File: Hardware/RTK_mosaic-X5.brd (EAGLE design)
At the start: 151.8 x 101.6 mm, 359 parts, among them J2 MAGJACK-POE, J3 MICRO-SD-PUSH-PUSH-EXT-PIN, J4 Vertical Qwiic Connector, J9 MAGJACK-POE, U1 ESP32-WROVER-IE, U10 POE_PSU-DP990X, U11 SN74AVC4T774PW, U17 URB2405YMD, U2 CH340C, U3 AP7361C-33FGEUDFN-8, U4 TXS0108, U5 TXS0108, U6 AP7361C-33FGEUDFN-8, U7 KSZ8041NL, U8 MOSAIC-X5X5, U9 KSZ8041NL

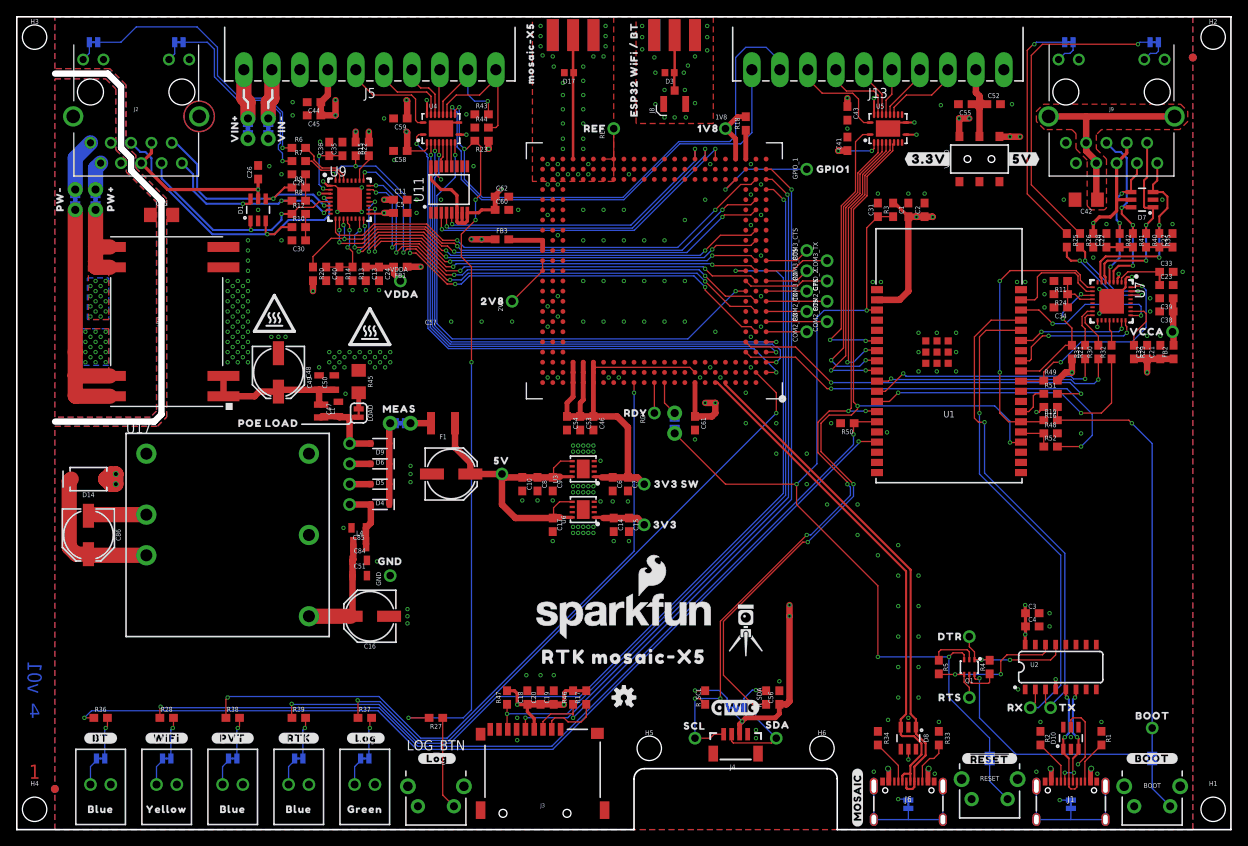
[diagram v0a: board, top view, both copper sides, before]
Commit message: Correct Ethernet PHY pad numbering. Needs re-panelizing
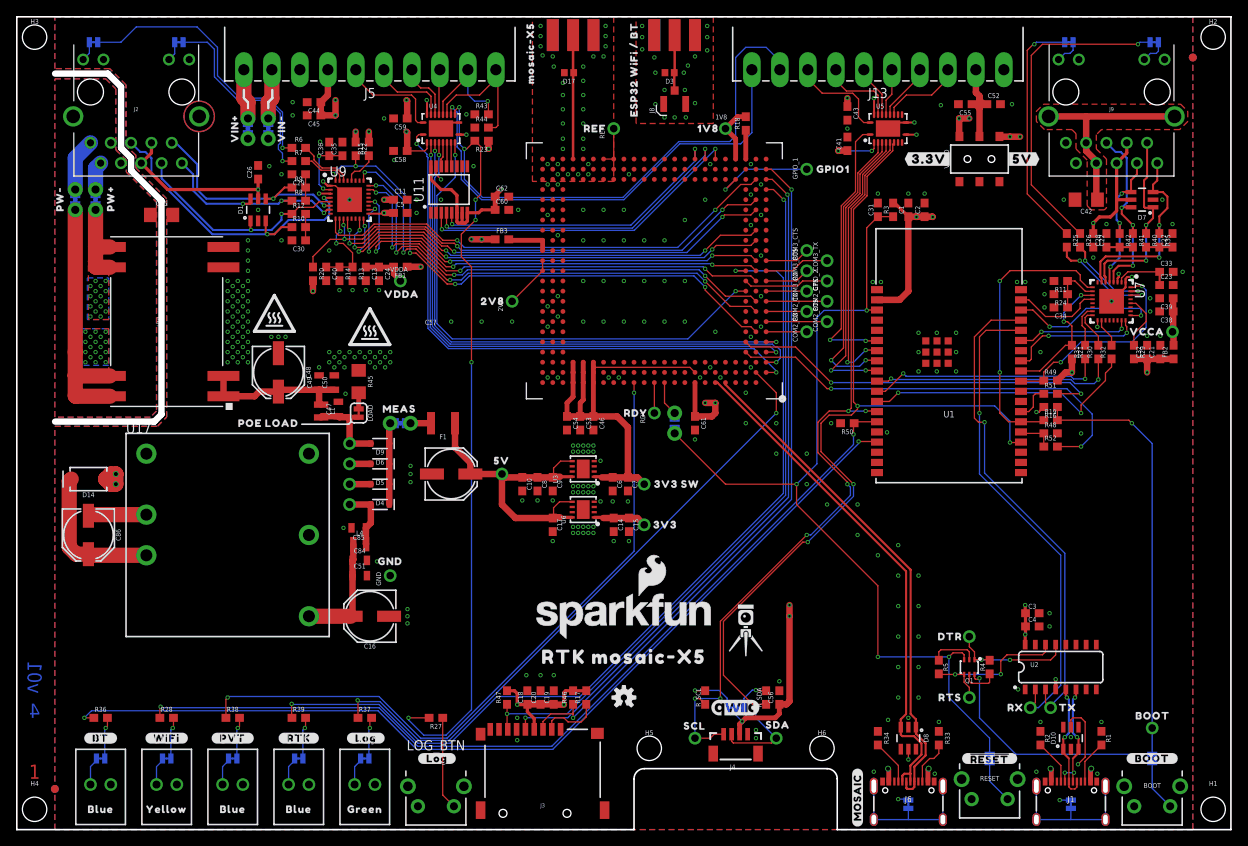
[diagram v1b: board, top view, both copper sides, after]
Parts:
- U7, U9: device Septentrio_Mosaic:MLF55Q-32LD -> Septentrio_mosaic-X5:MLF55Q-32LD
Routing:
- net ESP23_MDC: track 13.3 -> 11.1 mm
- net MOSAIC_LOG_BTN_IO: track 151.7 -> 153.6 mm
- net ESP27_CRSDV: track 36.8 -> 35.4 mm
- net ETHER_RXER: track 56.5 -> 57.6 mm
- net ETHER_MDC: track 59.2 -> 58.1 mm
- net N$147: track 9.87 -> 10.9 mm
- net ETHER_CRSDV: track 58.3 -> 57.5 mm
- net N$148: track 3.61 -> 4.39 mm
- net GND: vias 330 -> 329

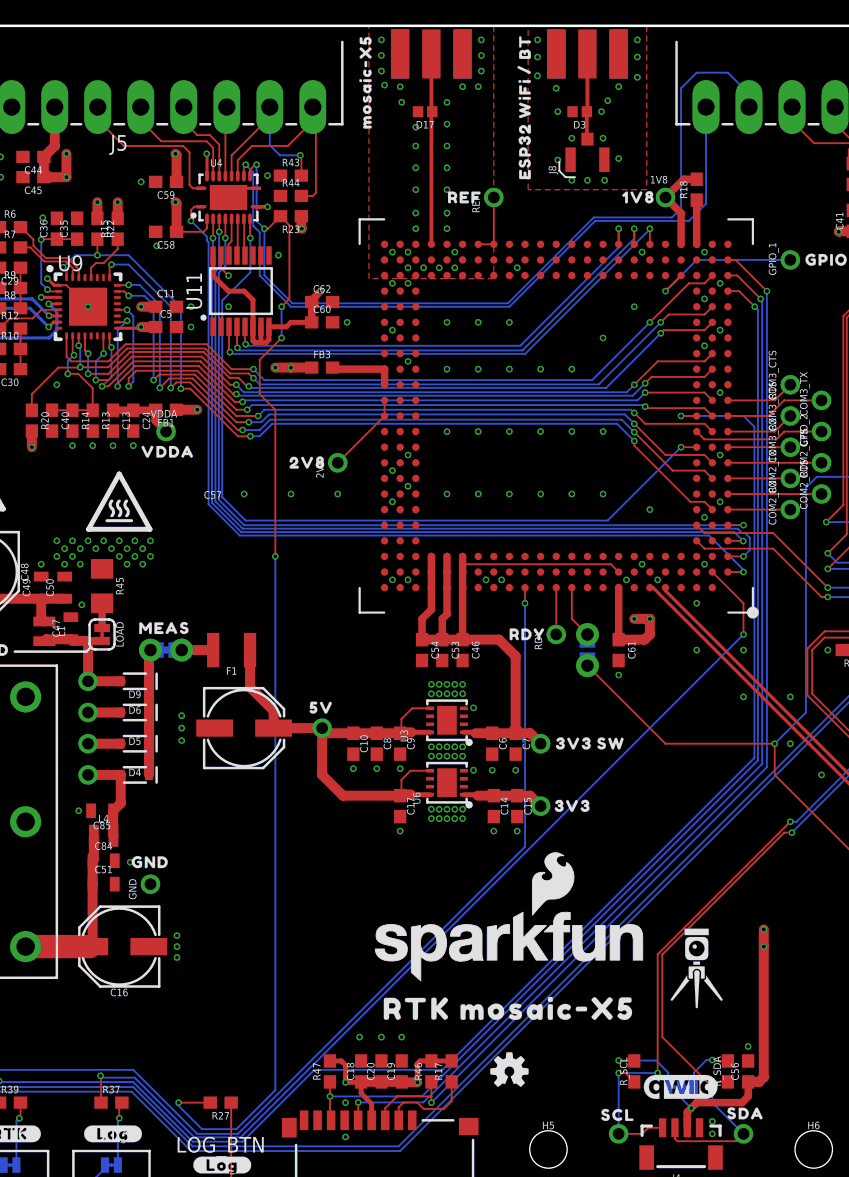
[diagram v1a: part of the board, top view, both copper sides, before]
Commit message: Add second antenna connector for future mosaic-H product
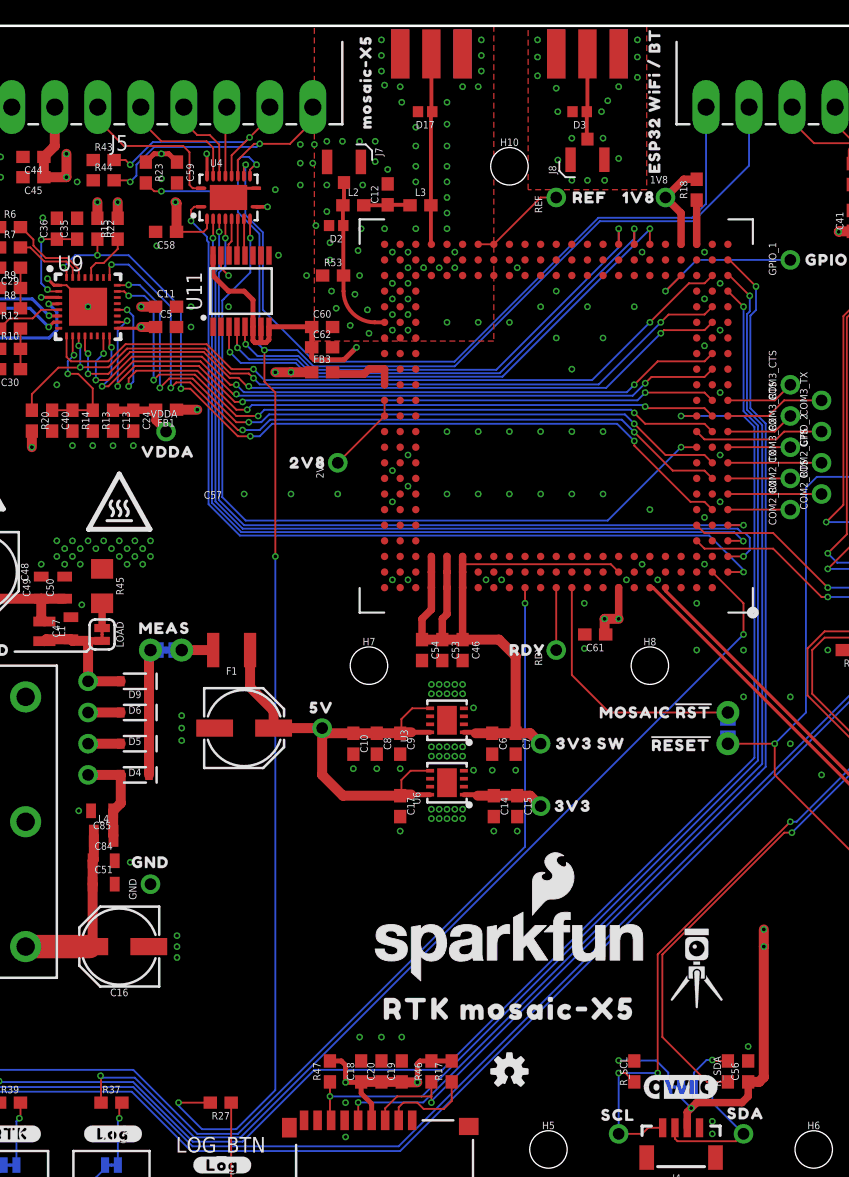
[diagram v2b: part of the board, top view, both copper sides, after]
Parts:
- added C12: DNP, SparkFun-Capacitors:0603_NO_CREAM
- added D2: PESD0402, SparkFun-DiscreteSemi:0402
- added H10, H7, H8: STAND-OFFTIGHT, SparkFun-Hardware:STAND-OFF-TIGHT
- added J7: (no value), SparkFun-Connectors:U.FL_REDUCED_FOOTPRINT
- added L2, L3: DNP, SparkFun-Coils:0603_NO-CREAM
- added R53: 0, SparkFun-Resistors:0603
- added U$4: (no value), output:#RESET#0
- added U$9: (no value), output:MOSAIC_#RST#6
- moved R43 15.3 mm to (43.2, 90.7)
- moved R44 15.3 mm to (43.2, 89.0)
- moved MOSAIC_RST 13.1 mm to (94.0, 44.5)
- moved R23 12.3 mm to (46.6, 89.7), turned to 270 degrees
- moved U$21 10.6 mm to (88.0, 102.1)
- moved U$79 10.2 mm to (84.8, 87.6)
- moved U$74 7.41 mm to (90.2, 43.2)
- moved U$73 6.35 mm to (82.9, 45.8)
- moved REF 5.08 mm to (80.0, 87.6)
- moved U$80 5.08 mm to (77.9, 86.1)
- moved C62 3.68 mm to (61.0, 75.4)
- moved C61 2.29 mm to (83.2, 52.1), turned to 180 degrees
- moved RDY 1.27 mm to (80.0, 50.8)
- moved U$75 1.27 mm to (79.9, 50.8)
- moved U$78 1.27 mm to (75.3, 50.8)
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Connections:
- removed net MOSAIC_RF: D17.1, MOSAIC_RF.SIG, U8.AC20
- new net ANT1: D17.1, L3.2, MOSAIC_RF.SIG, U8.AC20
- new net ANT2: D2.1, J7.FEED, L2.1, R53.2, U8.V23
- new net N$13: C12.1, L2.2, L3.1
- net GND: now also C12.2, D2.2, J7.1, J7.2, R53.1; no longer U8.V23
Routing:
- net MOSAIC_!RST!: track 5.10 -> 21.8 mm
- net MOSAIC_RF: track 15.7 -> 0.00 mm
- net ANT1: track 0.00 -> 15.6 mm
- net !RESET!: track 114.4 -> 100.3 mm
- net ANT2: track 0.00 -> 13.3 mm
- net MOSAIC_EVENTB_IO: track 18.2 -> 23.5 mm, vias 0 -> 2
- net MOSAIC_PPSO_IO: track 59.1 -> 64.3 mm
- net 5V: track 183.7 -> 178.6 mm
- net VCCIO: track 130.1 -> 135.1 mm, vias 7 -> 6
- net MOSAIC_EVENTA_IO: track 14.5 -> 19.0 mm, vias 1 -> 2
- net N$13: track 0.00 -> 3.83 mm
- net REF: track 5.08 -> 7.93 mm
- net 1.8V: track 58.3 -> 60.6 mm
- net MOSAIC_PPSO_1V8: track 38.0 -> 39.6 mm
- net MOSAIC_EVENTA_1V8: track 41.8 -> 43.4 mm
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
